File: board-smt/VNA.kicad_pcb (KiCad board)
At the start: 2 copper layers, 100 x 85 mm, 166 parts, among them J1 Conn_02x07_Odd_Even, J11 Conn_01x01, J13 Barrel_Jack, J14 Conn_01x01, J15 Conn_01x02, J16 Conn_01x01, J18 Conn_01x01, J19 Conn_01x01, J2 Conn_Coaxial, J20 Conn_01x01, J21 Conn_01x01, J24 USB_B, J3 Conn_01x01, J4 Conn_01x01, J5 Conn_01x01, J6 Conn_01x01, J7 Conn_01x01, J8 Conn_01x01, J9 Conn_Coaxial, Q3 S9018, SW1 SW_DPDT_x2, U1 SI5351A, U10 MT3608, U11 CN3052, U12 SI5351A, U2 LM339, U3 SA612, U4 SA612, U5 SA612, U6 LM358, U7 LM358, U8 AMS1117-3V3, U9 78M05_TO252, Y1 27 MHz

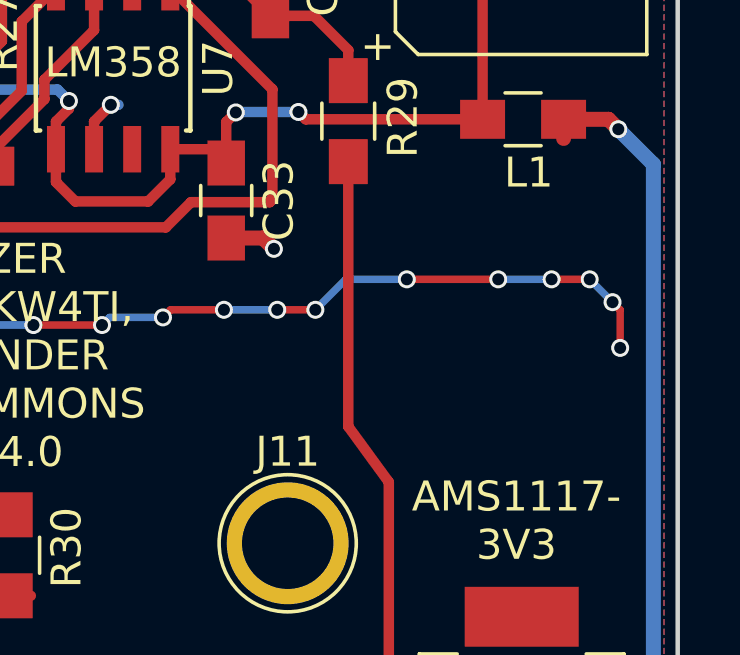
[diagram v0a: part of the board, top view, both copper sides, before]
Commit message: Forgot VNAOMizer logo
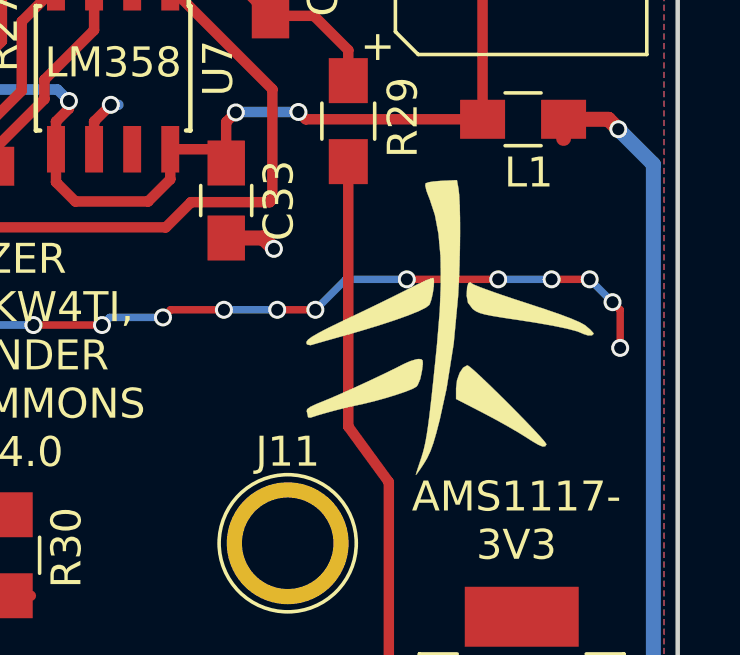
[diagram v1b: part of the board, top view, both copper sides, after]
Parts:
- added G***: LOGO, VNA:VNAOMizer, F.Cu at (142.4, 93.8)
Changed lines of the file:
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@@
     (tracks 2810)
     (zones 0)
-    (modules 166)
+    (modules 167)
     (nets 105)
   )
@@
   )
   (setup
-    (last_trace_width 0.5)
+    (last_trace_width 0.25)
     (user_trace_width 0.35)
     (user_trace_width 0.5)
@@
     )
   )
+  (module VNA:VNAOMizer (layer F.Cu)
+    (at 142.4 93.8)
+    (fp_text reference G*** (at 0 0) (layer F.SilkS) hide
+      (effects (font (thickness 0.3)))
+    )
+    (fp_text value LOGO (at 0.75 0) (layer F.SilkS) hide
+      (effects (font (thickness 0.3)))
+    )
+    (fp_poly (pts (xy 0.293123 -4.621389) (xy 0.317894 -4.398101) (xy 0.334924 -4.059111) (xy 0.344295 -3.629613)
+      (xy 0.34609 -3.134799) (xy 0.340391 -2.599861) (xy 0.327282 -2.049993) (xy 0.306845 -1.510387)
+      (xy 0.281376 -1.040503) (xy 0.132851 0.549482) (xy -0.105598 2.051599) (xy -0.329137 3.068511)
+      (xy -0.44618 3.524507) (xy -0.548457 3.872163) (xy -0.646898 4.141893) (xy -0.752432 4.364109)
+      (xy -0.859182 4.543478) (xy -0.990915 4.742234) (xy -1.086976 4.877522) (xy -1.128467 4.922866)
+      (xy -1.128889 4.921308) (xy -1.107542 4.840305) (xy -1.050995 4.66136) (xy -0.970491 4.419781)
+      (xy -0.951308 4.363564) (xy -0.898844 4.199208) (xy -0.851171 4.020657) (xy -0.806283 3.813472)
+      (xy -0.76217 3.563215) (xy -0.716825 3.255448) (xy -0.668239 2.875732) (xy -0.614404 2.40963)
+      (xy -0.553313 1.842704) (xy -0.482956 1.160514) (xy -0.422889 0.564444) (xy -0.332038 -0.538475)
+      (xy -0.293424 -1.515472) (xy -0.307325 -2.371822) (xy -0.374021 -3.1128) (xy -0.49379 -3.743681)
+      (xy -0.666911 -4.269739) (xy -0.680017 -4.300431) (xy -0.776027 -4.552624) (xy -0.816049 -4.729629)
+      (xy -0.80382 -4.798291) (xy -0.705213 -4.833254) (xy -0.507852 -4.863601) (xy -0.254079 -4.882859)
+      (xy -0.248985 -4.883076) (xy 0.2416 -4.903612) (xy 0.293123 -4.621389)) (layer F.SilkS) (width 0.01))
+    (fp_poly (pts (xy 0.668263 1.317823) (xy 0.82314 1.450533) (xy 1.041855 1.651986) (xy 1.308286 1.906042)
+      (xy 1.606316 2.196557) (xy 1.919825 2.507389) (xy 2.232692 2.822398) (xy 2.5288 3.12544)
+      (xy 2.792028 3.400373) (xy 3.006256 3.631056) (xy 3.155366 3.801346) (xy 3.223238 3.895102)
+      (xy 3.225398 3.905751) (xy 3.182105 3.970047) (xy 3.099226 3.976528) (xy 2.956451 3.918004)
+      (xy 2.733471 3.787287) (xy 2.540815 3.663418) (xy 2.271595 3.49674) (xy 1.919779 3.292474)
+      (xy 1.529298 3.075503) (xy 1.144085 2.87071) (xy 1.112065 2.854184) (xy 0.211667 2.390755)
+      (xy 0.211667 2.035297) (xy 0.243772 1.767589) (xy 0.32785 1.526408) (xy 0.445544 1.34856)
+      (xy 0.578497 1.270853) (xy 0.593341 1.27) (xy 0.668263 1.317823)) (layer F.SilkS) (width 0.01))
+    (fp_poly (pts (xy -0.946216 1.065488) (xy -0.900925 1.10942) (xy -0.896299 1.223823) (xy -0.922406 1.442396)
+      (xy -0.924452 1.457488) (xy -0.981931 1.726207) (xy -1.064968 1.924752) (xy -1.10667 1.978735)
+      (xy -1.230238 2.049751) (xy -1.462247 2.143052) (xy -1.773553 2.249581) (xy -2.135011 2.360284)
+      (xy -2.517475 2.466105) (xy -2.891801 2.557989) (xy -3.139722 2.610395) (xy -3.407776 2.668996)
+      (xy -3.736706 2.750557) (xy -4.078508 2.84215) (xy -4.385181 2.930848) (xy -4.608723 3.003724)
+      (xy -4.630389 3.011827) (xy -4.715506 3.006539) (xy -4.727222 2.976652) (xy -4.750819 2.849293)
+      (xy -4.767361 2.799718) (xy -4.751137 2.730729) (xy -4.640454 2.649848) (xy -4.418805 2.54681)
+      (xy -4.255833 2.481694) (xy -3.959586 2.360263) (xy -3.572416 2.19175) (xy -3.129516 1.99238)
+      (xy -2.666076 1.778374) (xy -2.217289 1.565958) (xy -1.818347 1.371353) (xy -1.541823 1.23054)
+      (xy -1.318736 1.13034) (xy -1.1183 1.068245) (xy -1.042105 1.058333) (xy -0.946216 1.065488)) (layer F.SilkS) (width 0.01))
+    (fp_poly (pts (xy -0.542509 -1.64788) (xy -0.521421 -1.549341) (xy -0.530529 -1.363452) (xy -0.56247 -1.138882)
+      (xy -0.609884 -0.924303) (xy -0.665407 -0.768384) (xy -0.679048 -0.745207) (xy -0.798112 -0.65308)
+      (xy -1.042072 -0.532947) (xy -1.398515 -0.389323) (xy -1.855024 -0.226725) (xy -2.399185 -0.04967)
+      (xy -3.018582 0.137325) (xy -3.421944 0.252633) (xy -3.804445 0.360157) (xy -4.142102 0.455712)
+      (xy -4.410267 0.532274) (xy -4.584297 0.582817) (xy -4.636768 0.598905) (xy -4.747126 0.577683)
+      (xy -4.770388 0.551681) (xy -4.777941 0.491533) (xy -4.724056 0.417029) (xy -4.596658 0.320843)
+      (xy -4.38367 0.195646) (xy -4.073018 0.034112) (xy -3.652626 -0.171087) (xy -3.316111 -0.330735)
+      (xy -2.868776 -0.543522) (xy -2.396326 -0.771903) (xy -1.941683 -0.994892) (xy -1.54777 -1.191506)
+      (xy -1.367319 -1.283497) (xy -1.066596 -1.433976) (xy -0.812523 -1.552478) (xy -0.630213 -1.62791)
+      (xy -0.544776 -1.649177) (xy -0.542509 -1.64788)) (layer F.SilkS) (width 0.01))
+    (fp_poly (pts (xy 0.731539 -1.46223) (xy 0.818222 -1.415777) (xy 1.020676 -1.333993) (xy 1.319994 -1.223676)
+      (xy 1.69727 -1.091624) (xy 2.1336 -0.944634) (xy 2.54 -0.811992) (xy 3.1671 -0.606363)
+      (xy 3.667291 -0.433407) (xy 4.050033 -0.289514) (xy 4.324785 -0.171074) (xy 4.501006 -0.074478)
+      (xy 4.533195 -0.051462) (xy 4.689368 0.081748) (xy 4.784372 0.186969) (xy 4.797778 0.217595)
+      (xy 4.741426 0.270517) (xy 4.610175 0.272792) (xy 4.460733 0.22468) (xy 4.445 0.215962)
+      (xy 4.245346 0.135201) (xy 3.909109 0.045705) (xy 3.440487 -0.051644) (xy 2.843679 -0.155962)
+      (xy 2.222161 -0.251889) (xy 1.762746 -0.320933) (xy 1.421289 -0.377361) (xy 1.175812 -0.426708)
+      (xy 1.004335 -0.474508) (xy 0.884877 -0.526294) (xy 0.795458 -0.587601) (xy 0.758473 -0.620418)
+      (xy 0.608861 -0.816858) (xy 0.564488 -1.055794) (xy 0.564445 -1.065764) (xy 0.58005 -1.332126)
+      (xy 0.624665 -1.477904) (xy 0.694992 -1.495271) (xy 0.731539 -1.46223)) (layer F.SilkS) (width 0.01))
+  )
   (gr_line (start 50 135) (end 50 50) (angle 90) (layer Edge.Cuts) (width 0.15))

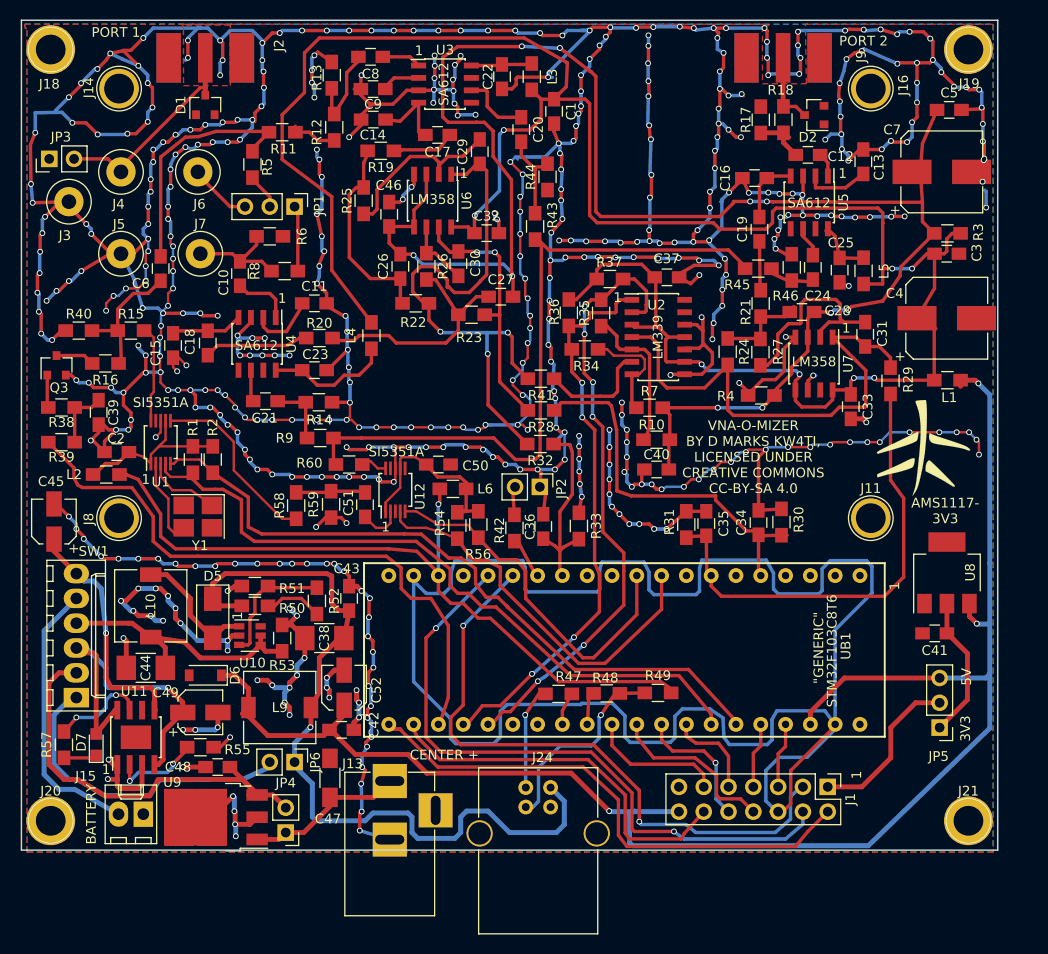
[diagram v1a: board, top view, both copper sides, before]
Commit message: Added SD card slot, reorganized pins
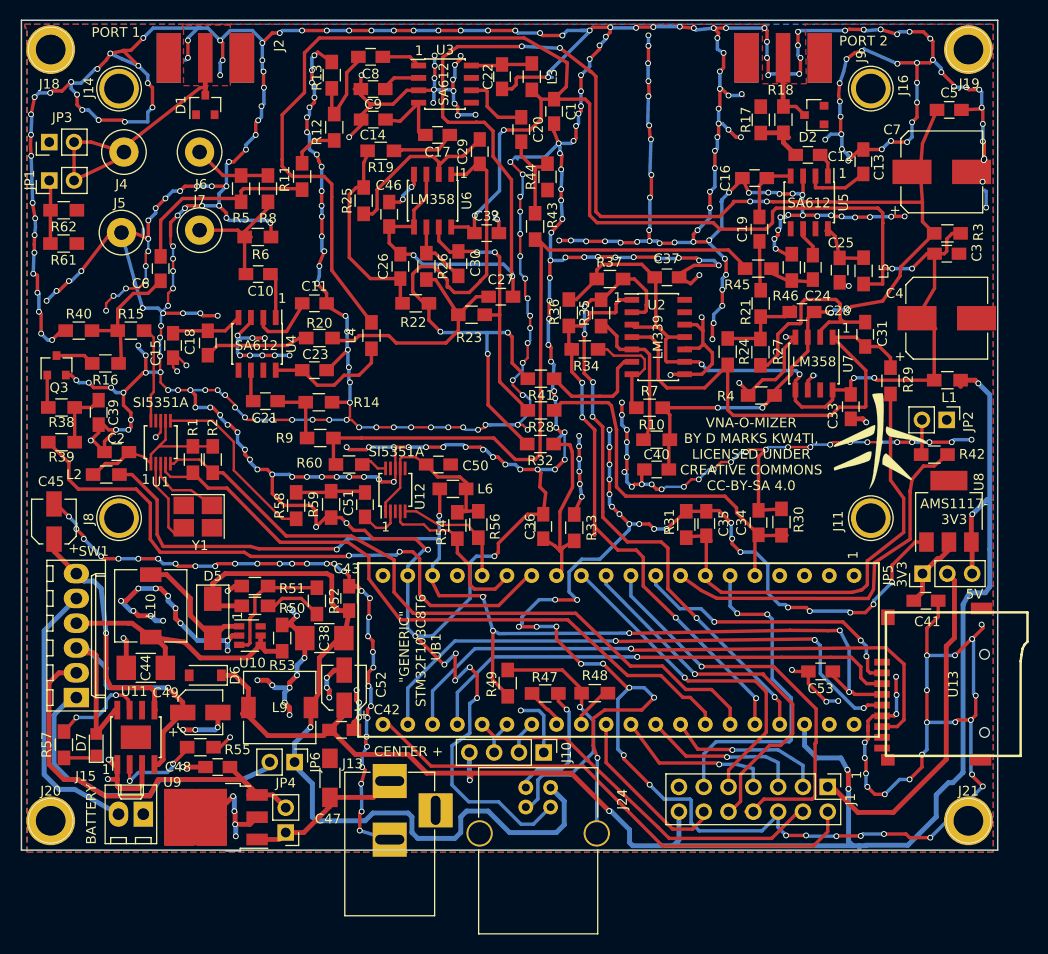
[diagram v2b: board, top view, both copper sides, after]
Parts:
- removed J3: Conn_01x01, Connectors:1pin
- added C53: 100 nF, Capacitors_SMD:C_0805_HandSoldering, F.Cu at (131.9, 116.7)
- added J10: Conn_01x04, Pin_Headers:Pin_Header_Straight_1x04_Pitch2.54mm, F.Cu at (103.5, 125.0)
- added R61: 100R, Resistors_SMD:R_0805_HandSoldering, F.Cu at (54.3, 72.9)
- added R62: 100R, Resistors_SMD:R_0805_HandSoldering, F.Cu at (54.3, 69.5)
- added U13: MicroSD_SPI_CD, VNA:GCT-MEM2055-00-190-01-A, F.Cu at (137.3, 118.0)
- JP1: value Jumper_NC_Dual -> Jumper_NC_Small; footprint Pin_Headers:Pin_Header_Straight_1x03_Pitch2.54mm -> Pin_Headers:Pin_Header_Straight_1x02_Pitch2.54mm
- moved R42 43.7 mm to (143.5, 94.5), turned to 0 degrees
- moved JP2 42.2 mm to (144.8, 90.9)
- moved JP1 25.3 mm to (52.9, 66.4), turned to 90 degrees
- moved JP5 15.9 mm to (142.3, 106.7), turned to 90 degrees
- moved R49 15.4 mm to (99.8, 117.9), turned to 90 degrees
- moved R8 8.61 mm to (75.2, 67.2), turned to 90 degrees
- moved U8 6.30 mm to (145.0, 100.3)
- moved R11 4.97 mm to (78.8, 66.0), turned to 270 degrees
- moved G*** 4.48 mm to (138.0, 93.1)
- moved C41 3.46 mm to (142.7, 109.5), turned to 0 degrees
- moved R5 2.74 mm to (72.5, 67.2), turned to 270 degrees
- moved J7 2.42 mm to (68.2, 71.5)
- moved J5 2.16 mm to (60.2, 71.8)
- moved J4 2.05 mm to (60.5, 63.5)
- moved J6 2.04 mm to (68.2, 63.5)
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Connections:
- J1 pad 10: Net-(J1-Pad10) -> MISO1
- J1 pad 11: Net-(J1-Pad11) -> PA1
- J1 pad 12: Net-(J1-Pad12) -> PA15
- J1 pad 3: PB10 -> PB5
- J1 pad 4: PB11 -> PA8
- J1 pad 5: Net-(J1-Pad5) -> PB4
- J1 pad 7: Net-(J1-Pad7) -> PB3
- J1 pad 8: Net-(J1-Pad8) -> SCK1
- J1 pad 9: Net-(J1-Pad9) -> MOSI1
- JP1 pad 2: Net-(JP1-Pad2) -> Net-(D1-Pad3)
- R42 pad 2: Net-(R42-Pad2) -> NODISPLAY
- R5 pad 1: Net-(JP1-Pad2) -> Net-(J6-Pad1)
- R8 pad 2: Net-(JP1-Pad1) -> Net-(J6-Pad1)
- UB1 pad 11: (no net) -> PA1
- UB1 pad 13: (no net) -> NODISPLAY
- UB1 pad 14: SCL2 -> SD_CS
- UB1 pad 15: SDA2 -> SCK1
- UB1 pad 16: (no net) -> MISO1
- UB1 pad 17: (no net) -> MOSI1
- UB1 pad 19: Net-(R42-Pad2) -> ATTEN
- UB1 pad 21: PB10 -> SCL2
- UB1 pad 22: PB11 -> SDA2
- UB1 pad 26: Net-(J1-Pad12) -> Net-(U13-Pad5)
- UB1 pad 27: ATTEN -> Net-(U13-Pad7)
- UB1 pad 28: SYNCSAMPLE -> Net-(U13-Pad3)
- UB1 pad 29: SYNCSAMPLE2 -> PA8
- UB1 pad 30: (no net) -> Net-(J10-Pad3)
- UB1 pad 31: (no net) -> Net-(J10-Pad2)
- UB1 pad 38: Net-(J1-Pad11) -> PA15
- UB1 pad 39: Net-(J1-Pad8) -> PB3
- UB1 pad 40: Net-(J1-Pad10) -> PB4
- UB1 pad 41: Net-(J1-Pad9) -> PB5
- UB1 pad 45: Net-(J1-Pad7) -> SYNCSAMPLE
- UB1 pad 46: Net-(J1-Pad5) -> SYNCSAMPLE2
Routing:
- net GND: track 1273.2 -> 1395.5 mm, vias 500 -> 555
- net PB11: track 65.9 -> 0.00 mm, vias 2 -> 0
- net PB10: track 64.0 -> 0.00 mm, vias 2 -> 0
- net Net-(U13-Pad7): track 0.00 -> 62.7 mm, vias 0 -> 1
- net Net-(U13-Pad5): track 0.00 -> 59.3 mm, vias 0 -> 3
- net Net-(U13-Pad3): track 0.00 -> 50.1 mm, vias 0 -> 1
- net SCK1: track 0.00 -> 42.8 mm, vias 0 -> 1
- net MISO1: track 0.00 -> 39.7 mm, vias 0 -> 1
- net NODISPLAY: track 0.00 -> 39.2 mm
- net PA8: track 0.00 -> 38.8 mm
- net Net-(J1-Pad12): track 38.7 -> 0.00 mm
- net +3V3: track 77.8 -> 116.5 mm, vias 1 -> 7
- net MOSI1: track 0.00 -> 35.2 mm, vias 0 -> 1
- net PA1: track 0.00 -> 34.8 mm, vias 0 -> 2
- net SD_CS: track 0.00 -> 29.4 mm, vias 0 -> 3
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
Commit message: Adds SD card support, which is mandatory.  Also changed firmware for new pinouts.
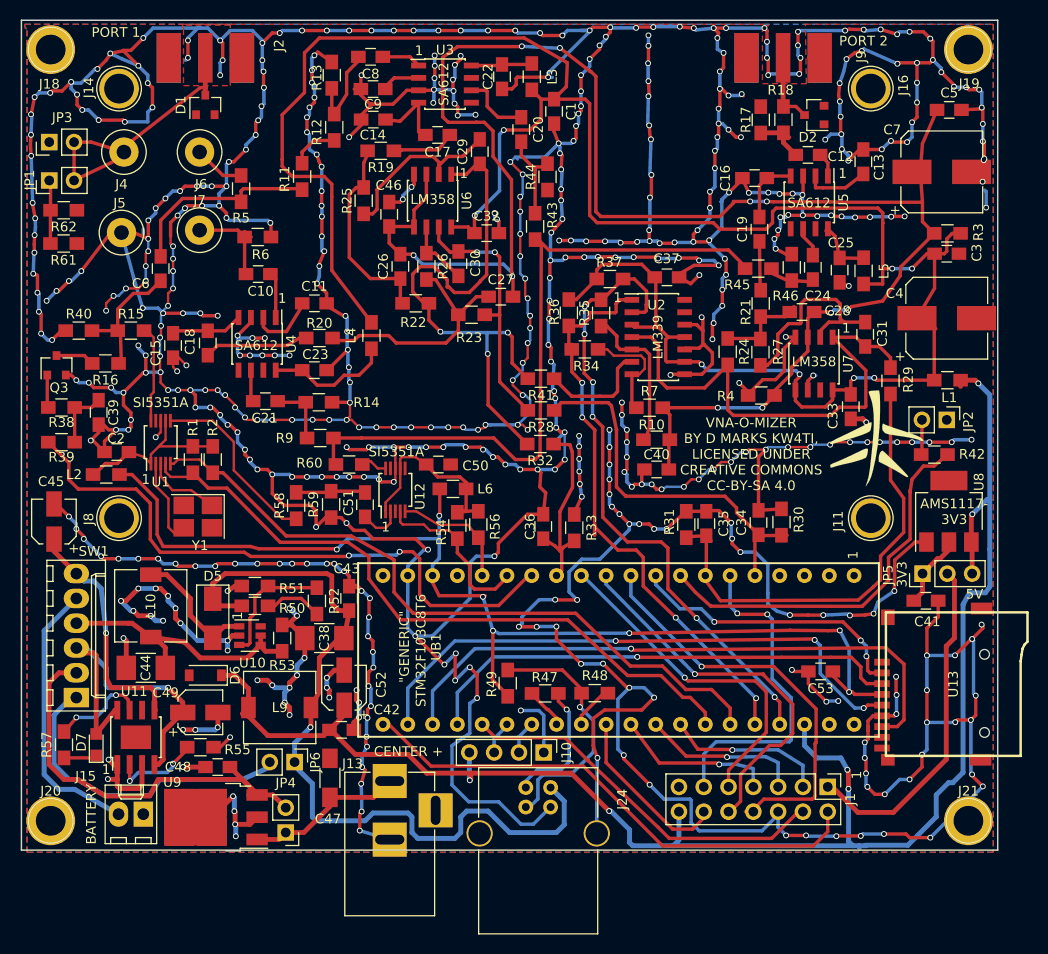
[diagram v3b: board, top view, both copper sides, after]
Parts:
- removed R8: 51R, Resistors_SMD:R_0805_HandSoldering
- R1, R2, R54, R56: value 10k -> 10k
- R43, R45, R9: value 1.5k -> 1k5
- moved G*** 0.47 mm to (137.6, 92.8)
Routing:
- net SAMPCUR: track 14.4 -> 10.4 mm
- net Net-(J6-Pad1): track 8.69 -> 5.94 mm
- net DEMODCUR2: track 47.1 -> 48.3 mm
- net GND: track 1395.5 -> 1396.7 mm
- net NODISPLAY: track 39.2 -> 40.0 mm
